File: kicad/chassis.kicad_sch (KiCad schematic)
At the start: 19 parts, among them J201 Left 1, J202 Right 1, J203 Left 2, J204 Right 2, J205 Left 3, J206 Right 3, J207 Mono 4, J208 Mono 5, J209 Left Out, J210 Right Out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

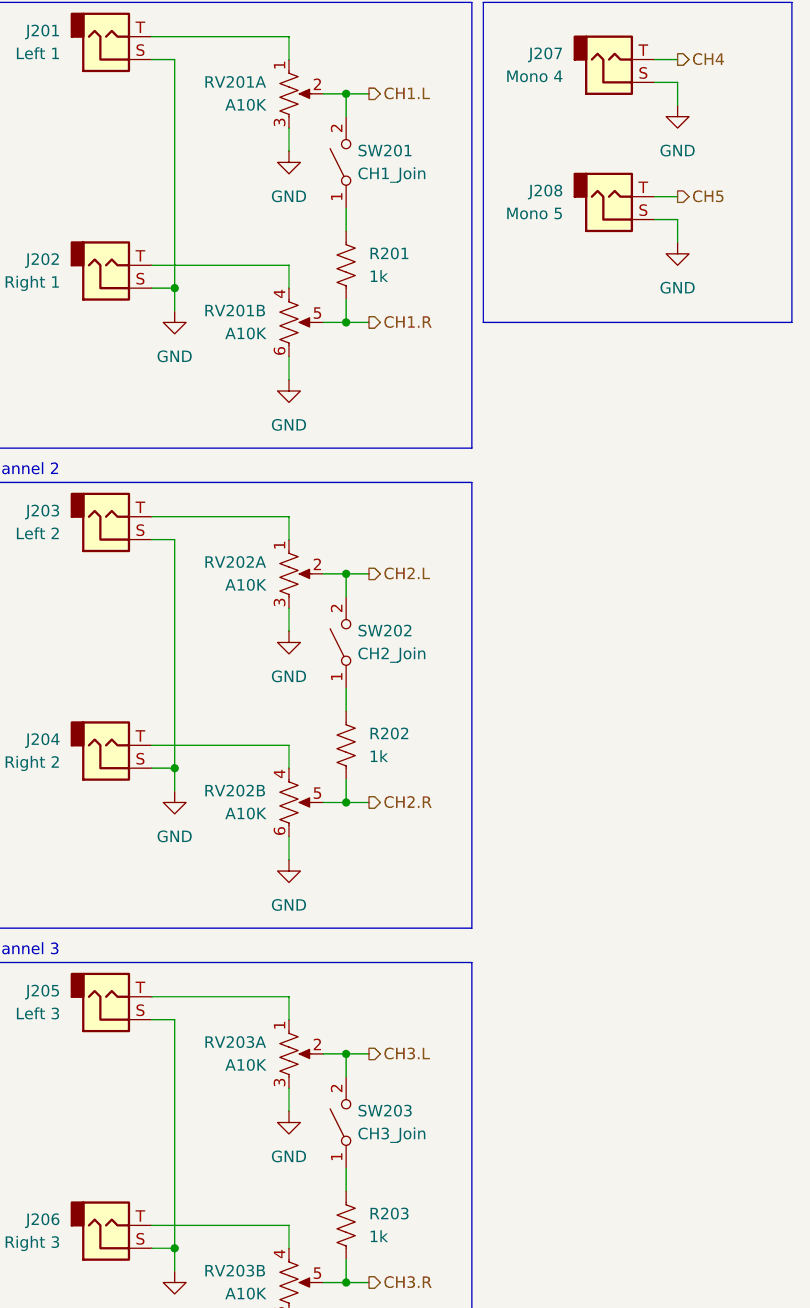
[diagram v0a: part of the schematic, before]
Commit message: replace electrolytic caps with ceramics
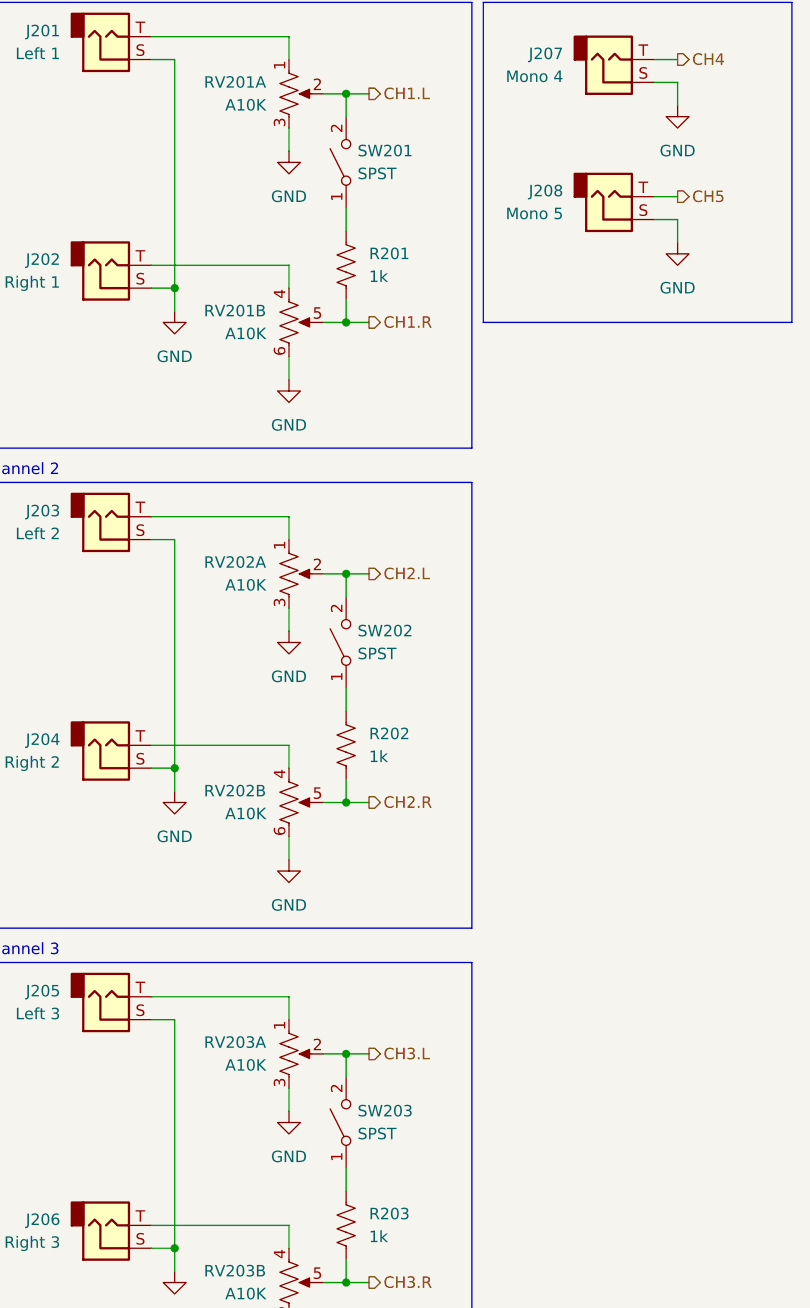
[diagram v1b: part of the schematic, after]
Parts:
- SW201: value CH1_Join -> SPST
- SW202: value CH2_Join -> SPST
- SW203: value CH3_Join -> SPST
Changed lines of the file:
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@@
 			)
 		)
-		(property "Value" "CH1_Join"
+		(property "Value" "SPST"
 			(at 55.88 35.5599 90)
 			(effects
@@
 			)
 		)
-		(property "Value" "CH2_Join"
+		(property "Value" "SPST"
 			(at 55.88 88.8999 90)
 			(effects
@@
 			)
 		)
-		(property "Value" "CH3_Join"
+		(property "Value" "SPST"
 			(at 55.88 142.2399 90)
 			(effects
